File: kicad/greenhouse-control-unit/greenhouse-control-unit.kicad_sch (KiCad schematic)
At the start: 43 parts, among them J1 Screw_Terminal_01x02, J10_Buck2 Conn_01x01_Female, J11_Buck2 Conn_01x01_Female, J12_Buck1 Conn_01x01_Female, J13_Buck1 Conn_01x01_Female, J14_Buck2 Conn_01x01_Female, J15_Buck2 Conn_01x01_Female, J16 Screw_Terminal_01x16, J2 Screw_Terminal_01x02, J3 Screw_Terminal_01x02, J4 Screw_Terminal_01x06, J5 Conn_01x03_Male, J6 Conn_01x02_Male, J6_BigBuck1 Conn_01x01_Female, J7_Buck1 Conn_01x01_Female, J8 Conn_01x15_Female, J9 Conn_01x15_Female, Q1 IRLB8721PBF, Q2 IRLB8721PBF, Q3 IRLB8721PBF, Q4 IRLB8721PBF, Q6 2N2222A, Q7 2N2222A, Q8 2N2222A, Q9 IRLB8721PBF, U1 74HC595, U2 74HC595

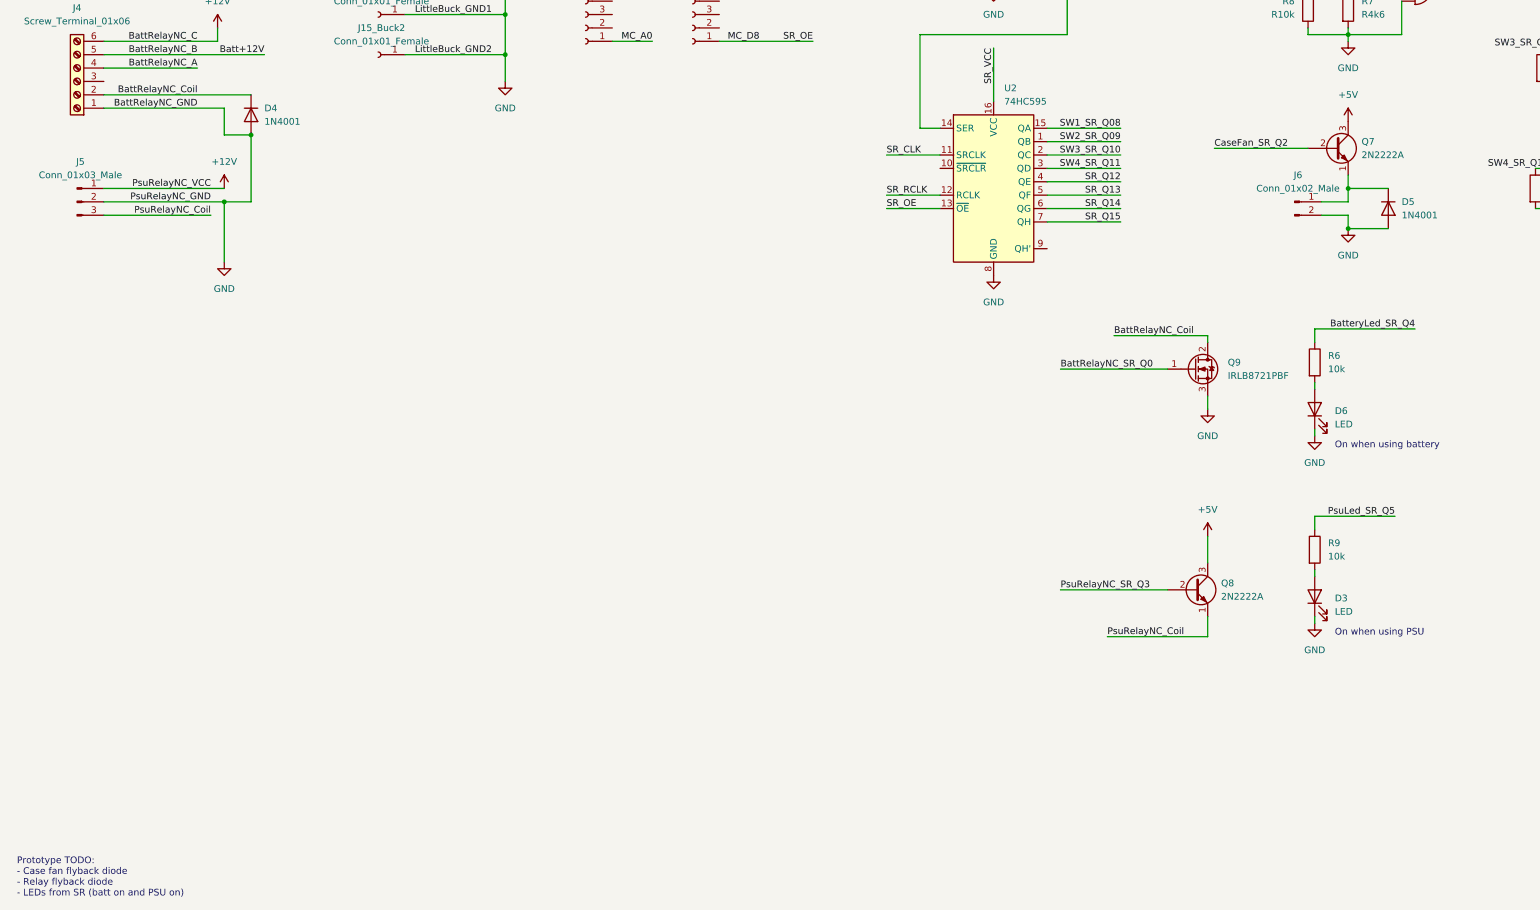
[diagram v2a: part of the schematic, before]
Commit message: Removed flyback diodes (for now)
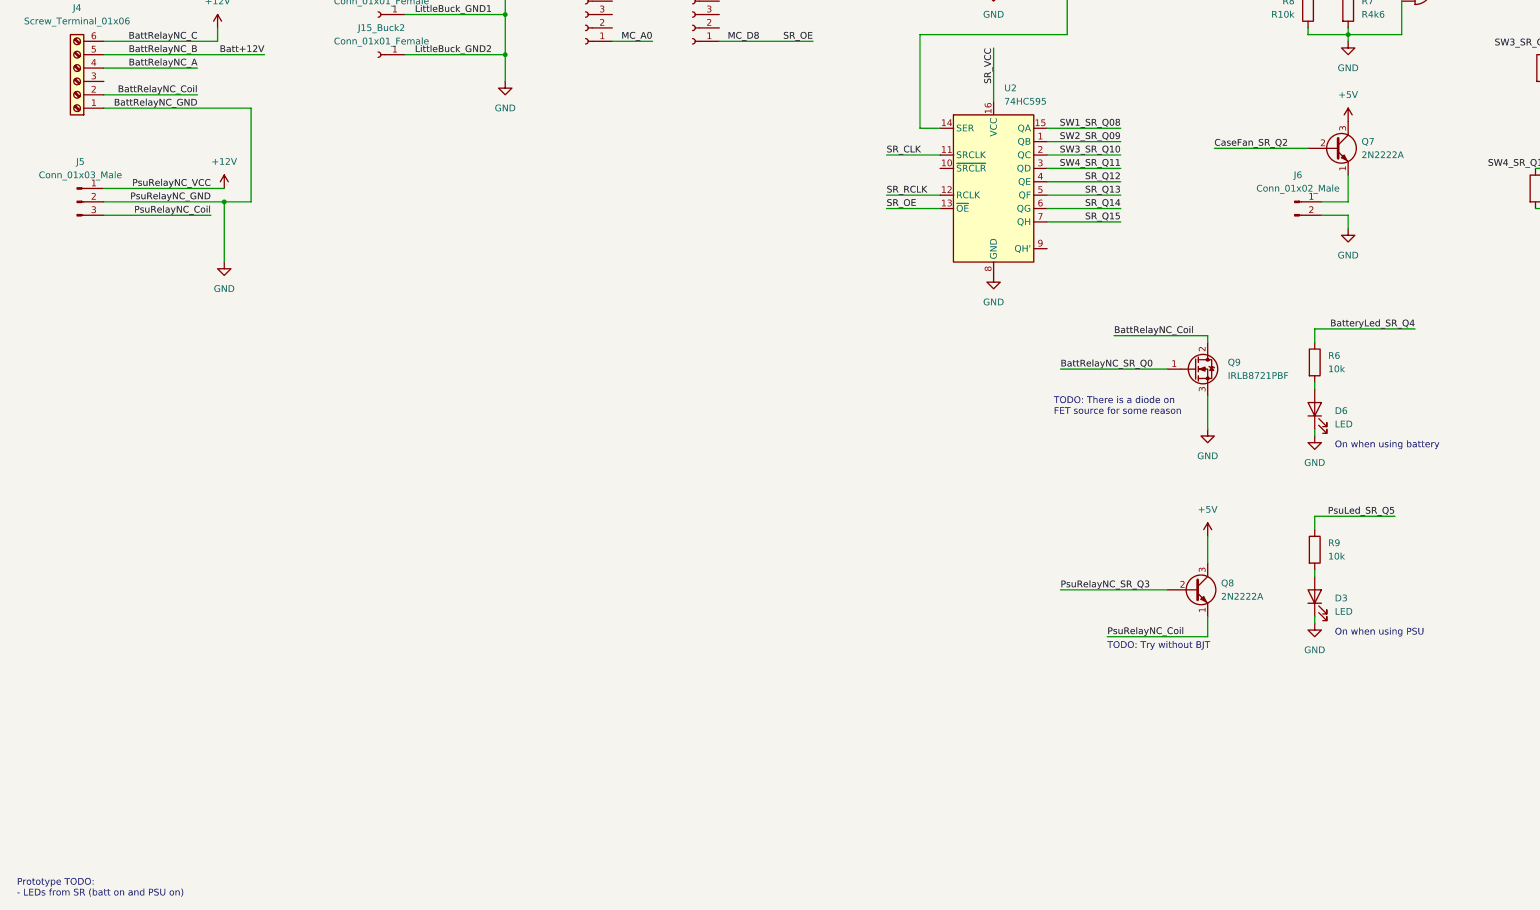
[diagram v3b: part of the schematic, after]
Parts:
- removed D4, D5: 1N4001, Diode_THT:D_DO-41_SOD81_P10.16mm_Horizontal, symbol Diode:1N4001
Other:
- note added: "Prototype TODO: - LEDs from SR (batt on and PSU on)"
- note added: "TODO: There is a diode on FET source for some reason"
- note added: "TODO: Try without BJT"
- note removed: "Prototype TODO: - Case fan flyback diode - Relay flyback diode - LEDs from SR (batt on and PSU on)"
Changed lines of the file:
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@@
   (junction (at 69.85 129.54) (diameter 0) (color 0 0 0 0)
   )
-  (junction (at 283.21 134.62) (diameter 0) (color 0 0 0 0)
-  )
   (junction (at 123.19 86.36) (diameter 0) (color 0 0 0 0)
   )
@@
   (junction (at 275.59 72.39) (diameter 0) (color 0 0 0 0)
   )
-  (junction (at 74.93 116.84) (diameter 0) (color 0 0 0 0)
-  )
-  (junction (at 283.21 127) (diameter 0) (color 0 0 0 0)
-  )
   (junction (at 330.2 107.95) (diameter 0) (color 0 0 0 0)
   )
@@
     (stroke (width 0) (type default) (color 0 0 0 0))
   )
-  (wire (pts (xy 283.21 127) (xy 290.83 127))
-    (stroke (width 0) (type default) (color 0 0 0 0))
-  )
   (wire (pts (xy 226.06 133.35) (xy 240.03 133.35))
     (stroke (width 0) (type default) (color 0 0 0 0))
@@
     (stroke (width 0) (type default) (color 0 0 0 0))
   )
-  (wire (pts (xy 46.99 109.22) (xy 74.93 109.22))
-    (stroke (width 0) (type default) (color 0 0 0 0))
-  )
-  (wire (pts (xy 283.21 127) (xy 283.21 129.54))
+  (wire (pts (xy 283.21 124.46) (xy 283.21 129.54))
     (stroke (width 0) (type default) (color 0 0 0 0))
   )
@@
     (stroke (width 0) (type default) (color 0 0 0 0))
   )
-  (wire (pts (xy 290.83 134.62) (xy 283.21 134.62))
-    (stroke (width 0) (type default) (color 0 0 0 0))
-  )
   (wire (pts (xy 276.86 200.66) (xy 276.86 199.39))
     (stroke (width 0) (type default) (color 0 0 0 0))
@@
     (stroke (width 0) (type default) (color 0 0 0 0))
   )
-  (wire (pts (xy 74.93 116.84) (xy 69.85 116.84))
-    (stroke (width 0) (type default) (color 0 0 0 0))
-  )
   (wire (pts (xy 339.09 49.53) (xy 330.2 49.53))
     (stroke (width 0) (type default) (color 0 0 0 0))
@@
     (stroke (width 0) (type default) (color 0 0 0 0))
   )
-  (wire (pts (xy 69.85 116.84) (xy 69.85 111.76))
-    (stroke (width 0) (type default) (color 0 0 0 0))
-  )
   (wire (pts (xy 163.83 66.04) (xy 181.61 66.04))
     (stroke (width 0) (type default) (color 0 0 0 0))
   )
+  (wire (pts (xy 46.99 109.22) (xy 64.77 109.22))
+    (stroke (width 0) (type default) (color 0 0 0 0))
+  )
   (wire (pts (xy 201.93 115.57) (xy 205.74 115.57))
     (stroke (width 0) (type default) (color 0 0 0 0))
@@
     (stroke (width 0) (type default) (color 0 0 0 0))
   )
-  (wire (pts (xy 283.21 124.46) (xy 283.21 127))
-    (stroke (width 0) (type default) (color 0 0 0 0))
-  )
   (wire (pts (xy 163.83 81.28) (xy 181.61 81.28))
     (stroke (width 0) (type default) (color 0 0 0 0))
@@
     (stroke (width 0) (type default) (color 0 0 0 0))
   )
-  (wire (pts (xy 74.93 129.54) (xy 74.93 116.84))
+  (wire (pts (xy 74.93 111.76) (xy 74.93 129.54))
     (stroke (width 0) (type default) (color 0 0 0 0))
   )
@@
     (stroke (width 0) (type default) (color 0 0 0 0))
   )
-  (wire (pts (xy 256.54 166.37) (xy 256.54 168.91))
+  (wire (pts (xy 256.54 166.37) (xy 256.54 172.72))
     (stroke (width 0) (type default) (color 0 0 0 0))
   )
@@
     (stroke (width 0) (type default) (color 0 0 0 0))
   )
-  (wire (pts (xy 46.99 111.76) (xy 69.85 111.76))
+  (wire (pts (xy 46.99 111.76) (xy 74.93 111.76))
     (stroke (width 0) (type default) (color 0 0 0 0))
   )
@@
     (effects (font (size 1.27 1.27)) (justify left bottom))
   )
-  (text "Prototype TODO:\n- Case fan flyback diode \n- Relay flyback diode\n- LEDs from SR (batt on and PSU on)"
+  (text "Prototype TODO:\n- LEDs from SR (batt on and PSU on)"
     (at 30.48 261.62 0)
     (effects (font (size 1.27 1.27)) (justify left bottom))
   )
+  (text "TODO: Try without BJT" (at 237.49 214.63 0)
+    (effects (font (size 1.27 1.27)) (justify left bottom))
+  )
   (text "On when using PSU" (at 280.67 212.09 0)
     (effects (font (size 1.27 1.27)) (justify left bottom))
   )
+  (text "TODO: There is a diode on \nFET source for some reason\n"
+    (at 227.33 170.18 0)
+    (effects (font (size 1.27 1.27)) (justify left bottom))
+  )
   (label "PsuRelayNC_GND" (at 67.31 129.54 180)
     (effects (font (size 1.27 1.27)) (justify right bottom))
@@
   (label "SR_CLK" (at 181.61 86.36 180)
     (effects (font (size 1.27 1.27)) (justify right bottom))
-  )
-  (symbol (lib_id "Diode:1N4001") (at 74.93 113.03 270) (unit 1)
-    (in_bom yes) (on_board yes) (fields_autoplaced)
-    (property "Reference" "D4" (id 0) (at 77.47 111.7599 90)
-      (effects (font (size 1.27 1.27)) (justify left))
-    )
-    (property "Value" "1N4001" (id 1) (at 77.47 114.2999 90)
-      (effects (font (size 1.27 1.27)) (justify left))
-    )
-    (property "Footprint" "Diode_THT:D_DO-41_SOD81_P10.16mm_Horizontal" (id 2) (at 70.485 113.03 0)
-      (effects (font (size 1.27 1.27)) hide)
-    )
-    (property "Datasheet" "http://www.vishay.com/docs/88503/1n4001.pdf" (id 3) (at 74.93 113.03 0)
-      (effects (font (size 1.27 1.27)) hide)
-    )
-    (pin "1")
-    (pin "2")
   )
   (symbol (lib_id "Connector:Conn_01x01_Female") (at 99.06 93.98 180) (unit 1)
@@
     )
     (pin "1")
-  )
-  (symbol (lib_id "Diode:1N4001") (at 290.83 130.81 270) (unit 1)
-    (in_bom yes) (on_board yes) (fields_autoplaced)
-    (property "Reference" "D5" (id 0) (at 293.37 129.5399 90)
-      (effects (font (size 1.27 1.27)) (justify left))
-    )
-    (property "Value" "1N4001" (id 1) (at 293.37 132.0799 90)
-      (effects (font (size 1.27 1.27)) (justify left))
-    )
-    (property "Footprint" "Diode_THT:D_DO-41_SOD81_P10.16mm_Horizontal" (id 2) (at 286.385 130.81 0)
-      (effects (font (size 1.27 1.27)) hide)
-    )
-    (property "Datasheet" "http://www.vishay.com/docs/88503/1n4001.pdf" (id 3) (at 290.83 130.81 0)
-      (effects (font (size 1.27 1.27)) hide)
-    )
-    (pin "1")
-    (pin "2")
   )
   (symbol (lib_id "power:+5VA") (at 123.19 57.15 0) (unit 1)
@@
     (pin "3")
   )
-  (symbol (lib_id "power:GND") (at 256.54 168.91 0) (unit 1)
+  (symbol (lib_id "power:GND") (at 256.54 172.72 0) (unit 1)
     (in_bom yes) (on_board yes)
-    (property "Reference" "#PWR0127" (id 0) (at 256.54 175.26 0)
-      (effects (font (size 1.27 1.27)) hide)
-    )
-    (property "Value" "GND" (id 1) (at 256.54 173.99 0))
-    (property "Footprint" "" (id 2) (at 256.54 168.91 0)
-      (effects (font (size 1.27 1.27)) hide)
-    )
-    (property "Datasheet" "" (id 3) (at 256.54 168.91 0)
+    (property "Reference" "#PWR0127" (id 0) (at 256.54 179.07 0)
+      (effects (font (size 1.27 1.27)) hide)
+    )
+    (property "Value" "GND" (id 1) (at 256.54 177.8 0))
+    (property "Footprint" "" (id 2) (at 256.54 172.72 0)
+      (effects (font (size 1.27 1.27)) hide)
+    )
+    (property "Datasheet" "" (id 3) (at 256.54 172.72 0)
       (effects (font (size 1.27 1.27)) hide)
     )
@@
       (reference "D3") (unit 1) (value "LED") (footprint "LED_THT:LED_D5.0mm")
     )
-    (path "/016bd694-0f47-4116-a7f6-772a7aecbe4f"
-      (reference "D4") (unit 1) (value "1N4001") (footprint "Diode_THT:D_DO-41_SOD81_P10.16mm_Horizontal")
-    )
-    (path "/1808f243-7e44-4c5b-9d98-2c4823e66ca8"
-      (reference "D5") (unit 1) (value "1N4001") (footprint "Diode_THT:D_DO-41_SOD81_P10.16mm_Horizontal")
-    )
     (path "/315bf0bf-415c-4adc-98f6-b8b86ec05949"

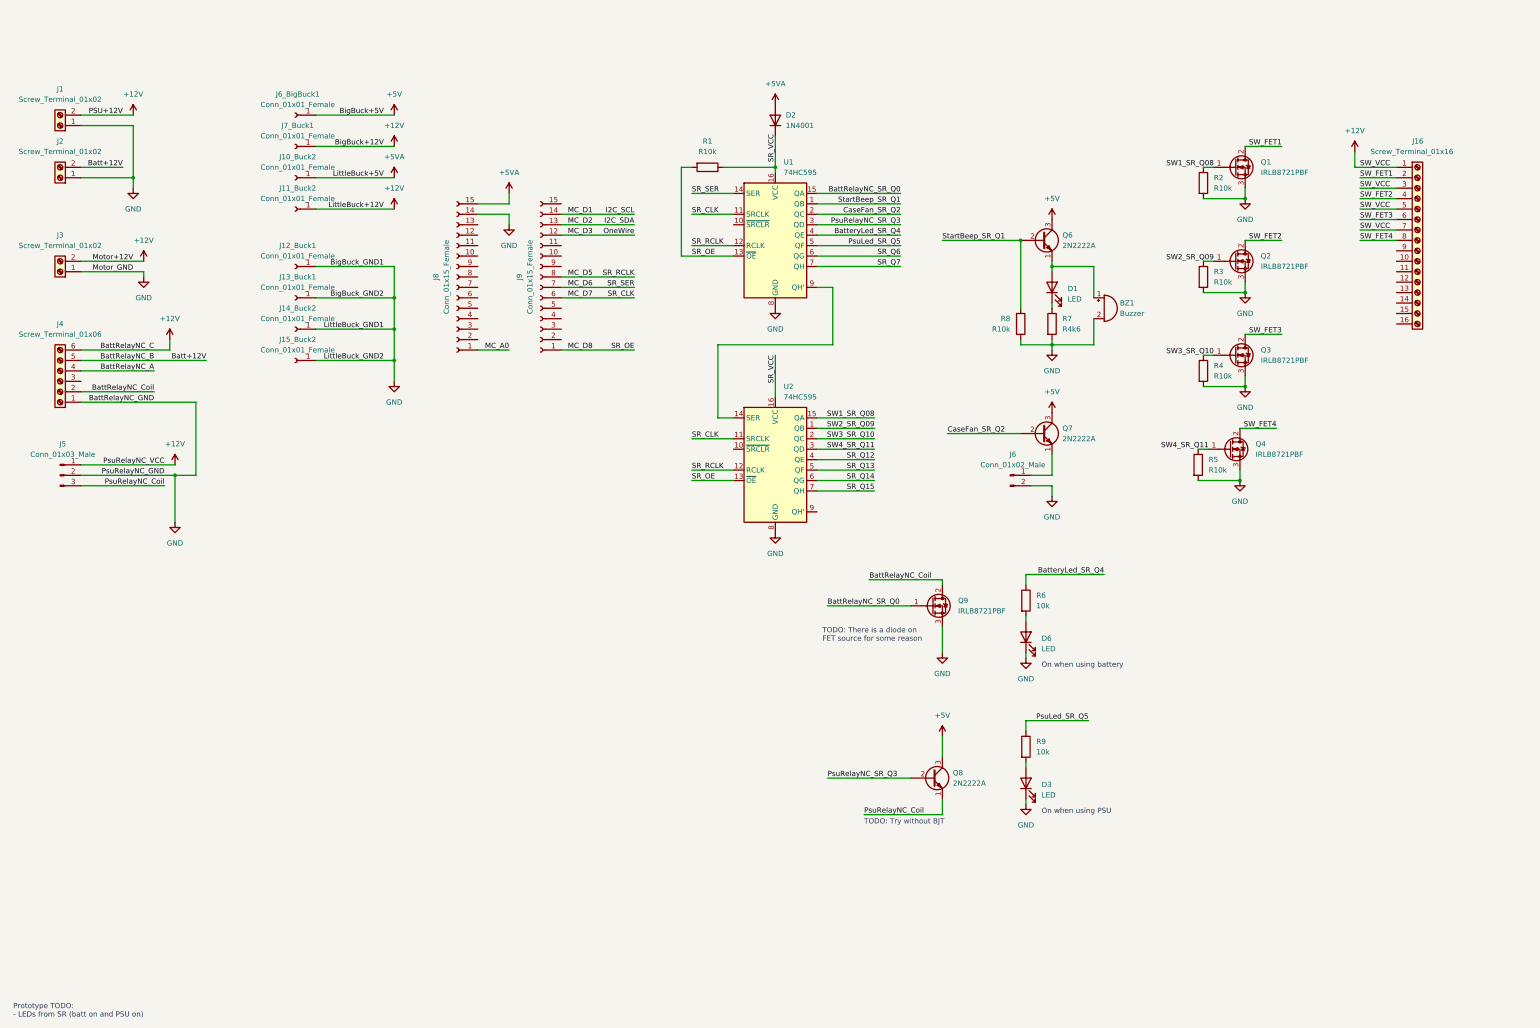
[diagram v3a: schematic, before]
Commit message: Rearranged PCB layout, re-annotate power connectors
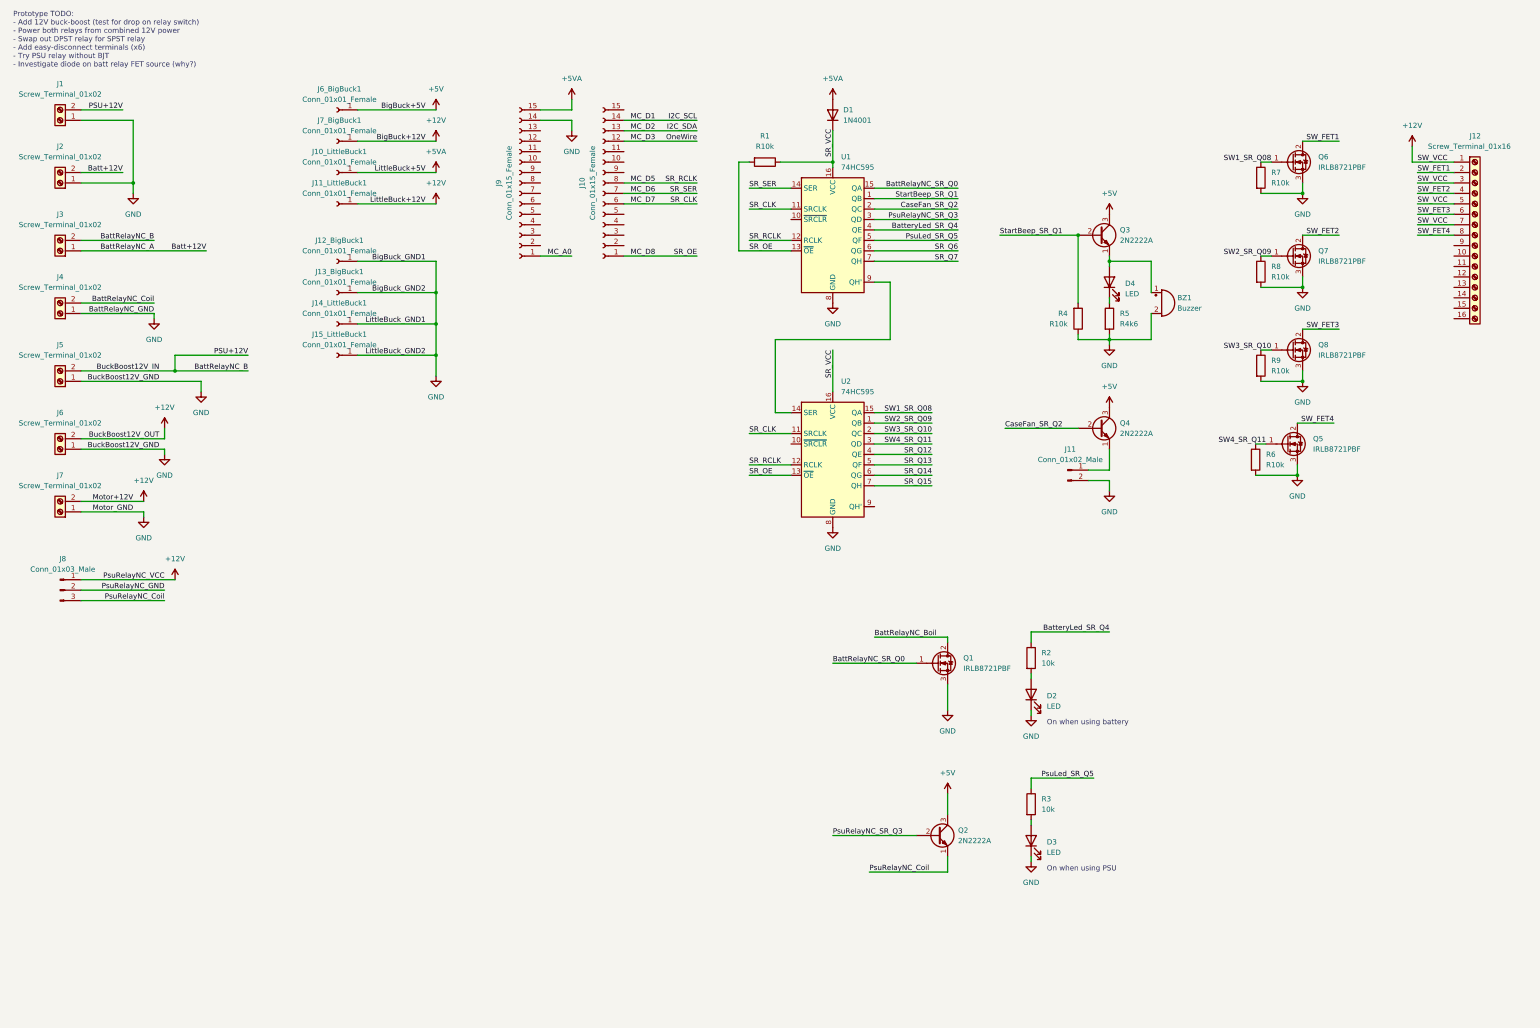
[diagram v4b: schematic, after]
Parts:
- removed J4: Screw_Terminal_01x06, TerminalBlock_Phoenix:TerminalBlock_Phoenix_MKDS-1,5-6-5.08_1x06_P5.08mm_Horizontal, symbol Connector:Screw_Terminal_01x06
- removed J5: Conn_01x03_Male, Connector_Molex:Molex_KK-254_AE-6410-03A_1x03_P2.54mm_Vertical, symbol Connector:Conn_01x03_Male
- added J3, J4, J5, J6: Screw_Terminal_01x02, TerminalBlock_Phoenix:TerminalBlock_Phoenix_MKDS-1,5-2-5.08_1x02_P5.08mm_Horizontal, symbol Connector:Screw_Terminal_01x02
- added J8: Conn_01x03_Male, Connector_Molex:Molex_KK-254_AE-6410-03A_1x03_P2.54mm_Vertical, symbol Connector:Conn_01x03_Male
- renumbered D2 to D1, D6 to D2, D1 to D4, J9 to J10, J10_Buck2 to J10_LittleBuck1, J6 to J11, J11_Buck2 to J11_LittleBuck1, J16 to J12, J12_Buck1 to J12_BigBuck1, J13_Buck1 to J13_BigBuck1, J14_Buck2 to J14_LittleBuck1, J15_Buck2 to J15_LittleBuck1, J3 to J7, J7_Buck1 to J7_BigBuck1, J8 to J9, Q9 to Q1, Q8 to Q2, Q6 to Q3, Q7 to Q4, Q4 to Q5, Q1 to Q6, Q2 to Q7, Q3 to Q8, R6 to R2, R9 to R3, R8 to R4, R7 to R5, R5 to R6, R2 to R7, R3 to R8, R4 to R9
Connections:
- net +12V: now also J6.2 (Pin_2), J8.1 (Pin_1); no longer J1.2 (Pin_2)
- net Batt+12V: now also J3.1 (Pin_1)
- net BattRelayNC_Coil: now also J4.2 (Pin_2); no longer Q1.2 (D)
- net GND: now also J4.1 (Pin_1), J5.1 (Pin_1), J6.1 (Pin_1)
- net PsuRelayNC_Coil: now also J8.3 (Pin_3)
- new net BattRelayNC_B: J1.2 (Pin_2), J3.2 (Pin_2), J5.2 (Pin_2)
- new net BattRelayNC_Boil: Q1.2 (D)
- new net PsuRelayNC_GND: J8.2 (Pin_2)
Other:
- note added: "Prototype TODO: - Add 12V buck-boost (test for drop on relay switch) - Power both relays from combined 12V power - Swap out DPST relay for SPST relay - Add easy-disconnect terminals (x6) - Try PSU relay without BJT - Investigate diode on batt relay FET source (why?)"
- note removed: "Prototype TODO: - LEDs from SR (batt on and PSU on)"
- note removed: "TODO: There is a diode on FET source for some reason"
- note removed: "TODO: Try without BJT"
- moved on the sheet: BZ1, D1, D2, D3, D4, J1, J10, J10_LittleBuck1, J11, J11_LittleBuck1, J12, J12_BigBuck1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

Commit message: Symbol position tweaks
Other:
- note added: "Prototype TODO: - Power both relays from combined 12V power - Reduce sensor pin headers to single block - Swap out DPST relay for SPST relay - Add easy-disconnect terminals (x6) - Try PSU relay without BJT - Investigate diode on batt relay FET source (why?) - Reverse MC direction (rotate 90deg)"
- note added: "Schematic TODO: - Diode/FET to block battery/PSU connection - Voltage sensor/divider behind PSU diode"
- note removed: "Prototype TODO: - Add 12V buck-boost (test for drop on relay switch) - Power both relays from combined 12V power - Swap out DPST relay for SPST relay - Add easy-disconnect terminals (x6) - Try PSU relay without BJT - Investigate diode on batt relay FET source (why?)"
- moved on the sheet: BZ1, D1, D2, D3, D4, J1, J10, J10_LittleBuck1, J11, J11_LittleBuck1, J12, J12_BigBuck1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
